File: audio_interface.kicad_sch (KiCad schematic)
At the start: 26 parts, among them J1 AudioJack2, J2 XLR3_Ground, U1 OPA1655D, U2 OPA1655D, U3 OPA1655D

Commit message: ADC semi-implmentation and MCU addition
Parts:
- J1: footprint Connector_Audio:Jack_6.35mm_Neutrik_NJ2FD-V_Vertical -> Connector_Audio:Jack_6.35mm_Neutrik_NMJ4HCD2_Horizontal
- J2: footprint Connector_Audio:Jack_XLR-6.35mm_Neutrik_NCJ5FI-H-0_Horizontal -> Connector_Audio:Jack_XLR-6.35mm_Neutrik_NCJ6FI-H_Horizontal
- RV1, RV2: footprint Potentiometer_THT:Potentiometer_ACP_CA6-H2,5_Horizontal -> Potentiometer_THT:Potentiometer_Alps_RK09K_Single_Horizontal
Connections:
- net MIC_AMP_OUT: now reaches RV1.3, U2.6
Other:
- added sheet adc (adc.kicad_sch)
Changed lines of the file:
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@@
 		(color 0 0 0 0)
 	)
+	(junction
+		(at 142.24 39.37)
+		(diameter 0)
+		(color 0 0 0 0)
+	)
 	(wire
 		(pts
@@
 	(wire
 		(pts
+			(xy 142.24 39.37) (xy 152.4 39.37)
+		)
+		(stroke
+			(width 0)
+			(type default)
+		)
+	)
+	(wire
+		(pts
 			(xy 67.31 39.37) (xy 68.58 39.37)
 		)
@@
 		)
 	)
+	(label "MIC_AMP_OUT"
+		(at 152.4 39.37 0)
+		(effects
+			(font
+				(size 1.27 1.27)
+			)
+			(justify left bottom)
+		)
+	)
 	(symbol
 		(lib_id "power:GND")
@@
 			)
 		)
-		(property "Footprint" "Connector_Audio:Jack_XLR-6.35mm_Neutrik_NCJ5FI-H-0_Horizontal"
+		(property "Footprint" "Connector_Audio:Jack_XLR-6.35mm_Neutrik_NCJ6FI-H_Horizontal"
 			(at 30.48 34.29 0)
 			(hide yes)
@@
 			)
 		)
-		(property "Footprint" "Connector_Audio:Jack_6.35mm_Neutrik_NJ2FD-V_Vertical"
+		(property "Footprint" "Connector_Audio:Jack_6.35mm_Neutrik_NMJ4HCD2_Horizontal"
 			(at 30.48 111.76 0)
 			(hide yes)
@@
 			)
 		)
-		(property "Footprint" "Potentiometer_THT:Potentiometer_ACP_CA6-H2,5_Horizontal"
+		(property "Footprint" "Potentiometer_THT:Potentiometer_Alps_RK09K_Single_Horizontal"
 			(at 76.2 139.7 0)
 			(hide yes)
@@
 			)
 		)
-		(property "Footprint" "Potentiometer_THT:Potentiometer_ACP_CA6-H2,5_Horizontal"
+		(property "Footprint" "Potentiometer_THT:Potentiometer_Alps_RK09K_Single_Horizontal"
 			(at 130.81 64.77 0)
 			(hide yes)
@@
 				)
 			)
+		)
+	)
+	(sheet
+		(at 16.51 186.69)
+		(size 25.4 6.35)
+		(exclude_from_sim no)
+		(in_bom yes)
+		(on_board yes)
+		(dnp no)
+		(fields_autoplaced yes)
+		(stroke
+			(width 0.1524)
+			(type solid)
+		)
+		(fill
+			(color 0 0 0 0)
+		)
+		(property "Sheetname" "adc"
+			(at 16.51 185.9784 0)
+			(show_name no)
+			(do_not_autoplace no)
+			(effects
+				(font
+					(size 1.27 1.27)
+				)
+				(justify left bottom)
+			)
+		)
+		(property "Sheetfile" "adc.kicad_sch"
+			(at 16.51 193.6246 0)
+			(show_name no)
+			(do_not_autoplace no)
+			(effects
+				(font
+					(size 1.27 1.27)
+				)
+				(justify left top)
+			)
+		)
+		(instances
+			(project "audio_interface"
+				(path "/4c5dcd2b-24fc-41d0-b8be-9f044db4ca6e"
+					(page "2")
+				)
+			)

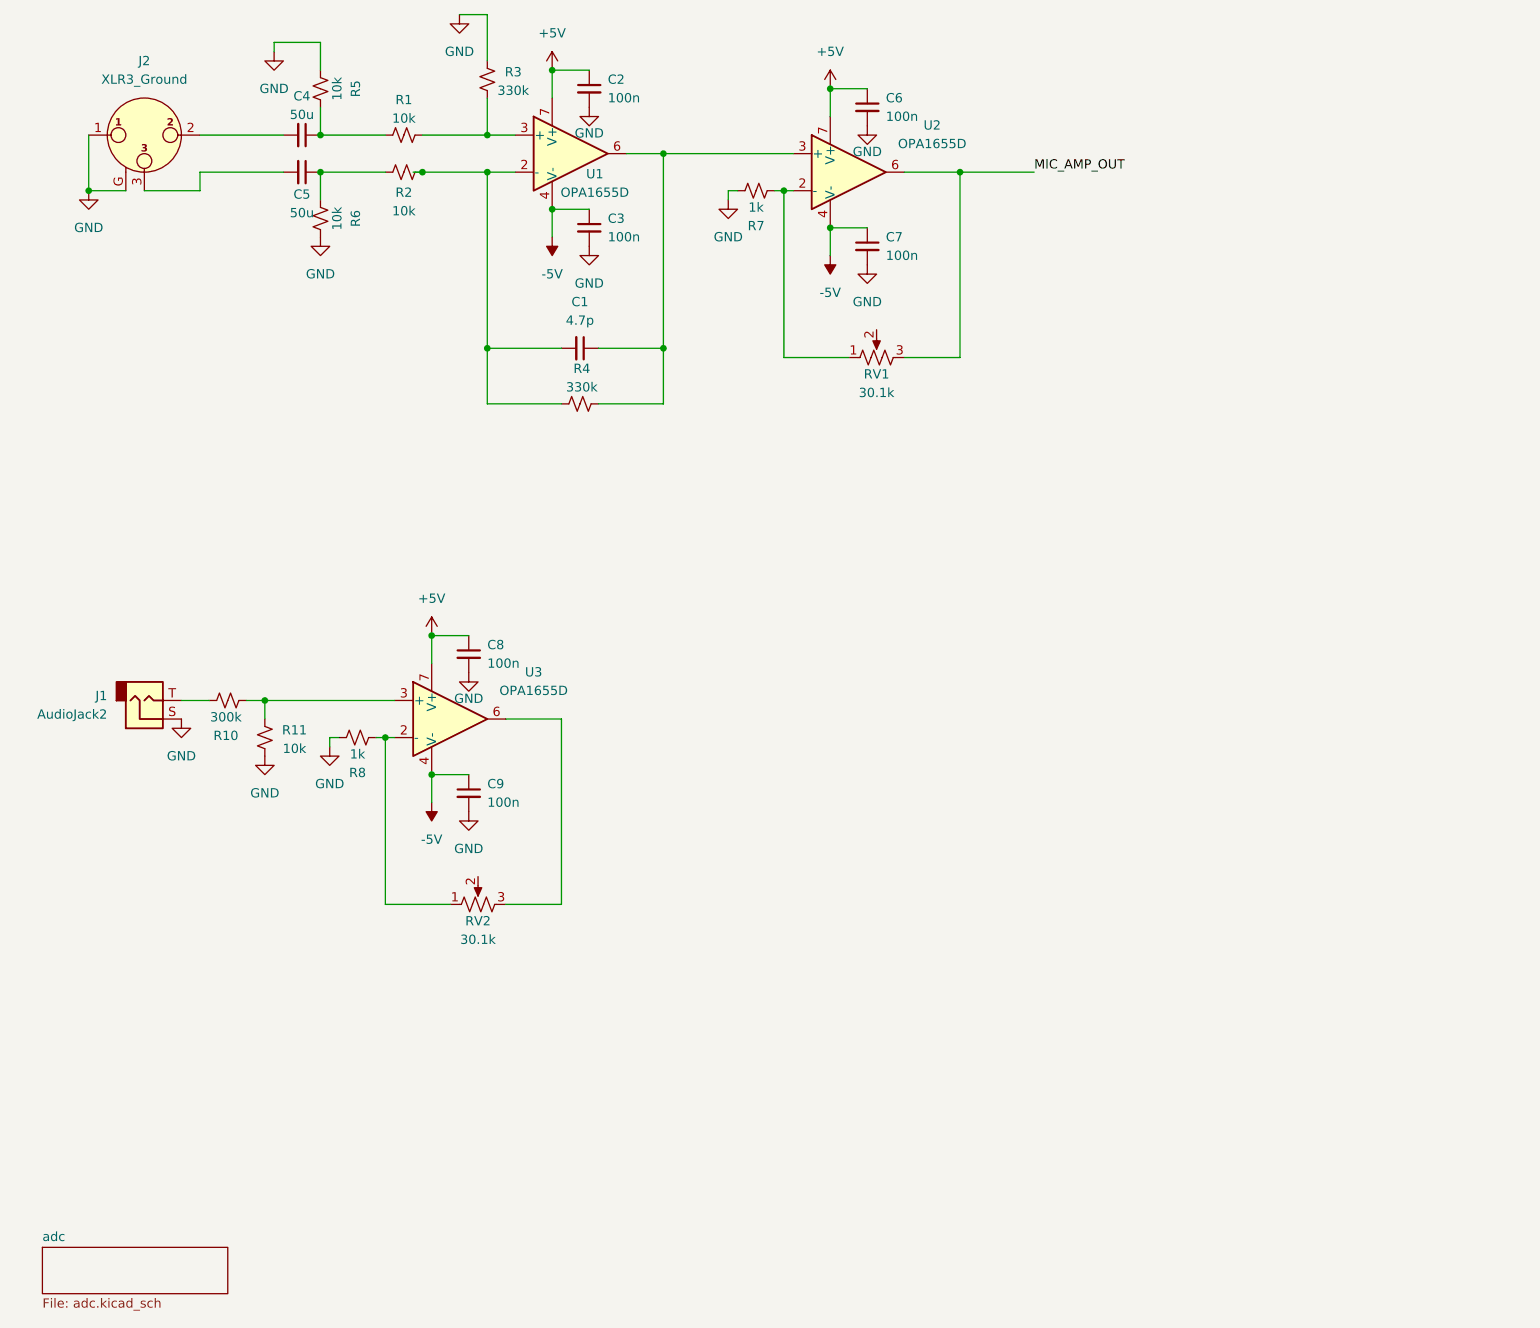
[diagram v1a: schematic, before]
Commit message: implementing full adc and semi-microcontroller
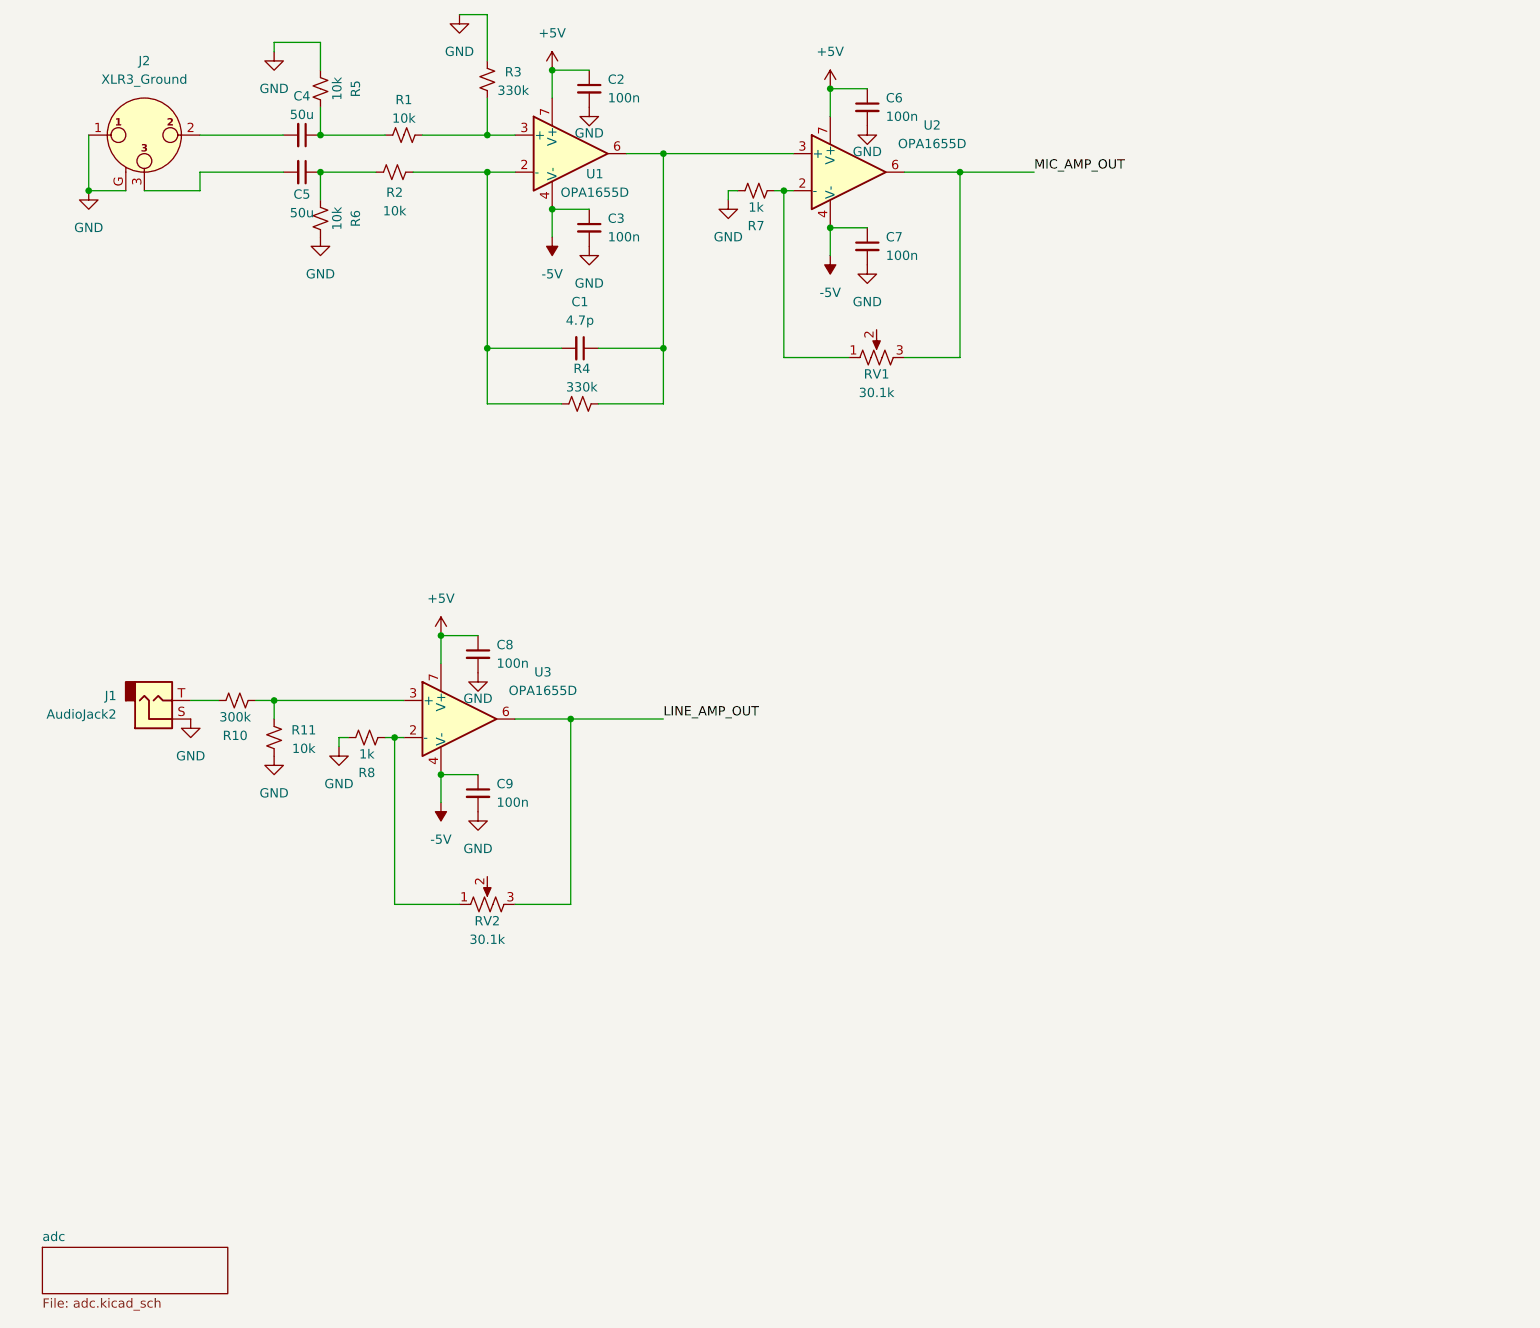
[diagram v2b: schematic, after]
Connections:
- net LINE_AMP_OUT: now reaches RV2.3, U3.6
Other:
- moved on the sheet: C8, C9, J1, R10, R11, R2, R8, RV2, U3

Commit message: wow... just wow...
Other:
- added sheet power (power.kicad_sch)
- moved on the sheet: C1, C2, C3, C4, C5, C6, C7, C8, C9, J1, J2, R1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

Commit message: Added DAC Page.
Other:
- added sheet DAC (DAC.kicad_sch)
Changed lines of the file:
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@@
+	)
+	(sheet
+		(at 16.51 167.64)
+		(size 12.7 3.81)
+		(exclude_from_sim no)
+		(in_bom yes)
+		(on_board yes)
+		(dnp no)
+		(stroke
+			(width 0.1524)
+			(type solid)
+		)
+		(fill
+			(color 0 0 0 0)
+		)
+		(property "Sheetname" "DAC"
+			(at 16.51 166.9284 0)
+			(show_name no)
+			(do_not_autoplace no)
+			(effects
+				(font
+					(size 1.27 1.27)
+				)
+				(justify left bottom)
+			)
+		)
+		(property "Sheetfile" "DAC.kicad_sch"
+			(at 16.51 172.0346 0)
+			(show_name no)
+			(do_not_autoplace no)
+			(effects
+				(font
+					(size 1.27 1.27)
+				)
+				(justify left top)
+			)
+		)
+		(instances
+			(project "audio_interface"
+				(path "/4c5dcd2b-24fc-41d0-b8be-9f044db4ca6e"
+					(page "4")
+				)
+			)
+		)
 	)
 	(sheet
